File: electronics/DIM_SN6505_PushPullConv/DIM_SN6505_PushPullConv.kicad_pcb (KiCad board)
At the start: 2 copper layers, 31.3 x 13.4 mm, 18 parts, among them J1 Conn_01x04, J2 Conn_01x04, J3 Conn_01x04, J4 Conn_01x04, T1 STR7040, U1 SN6506A

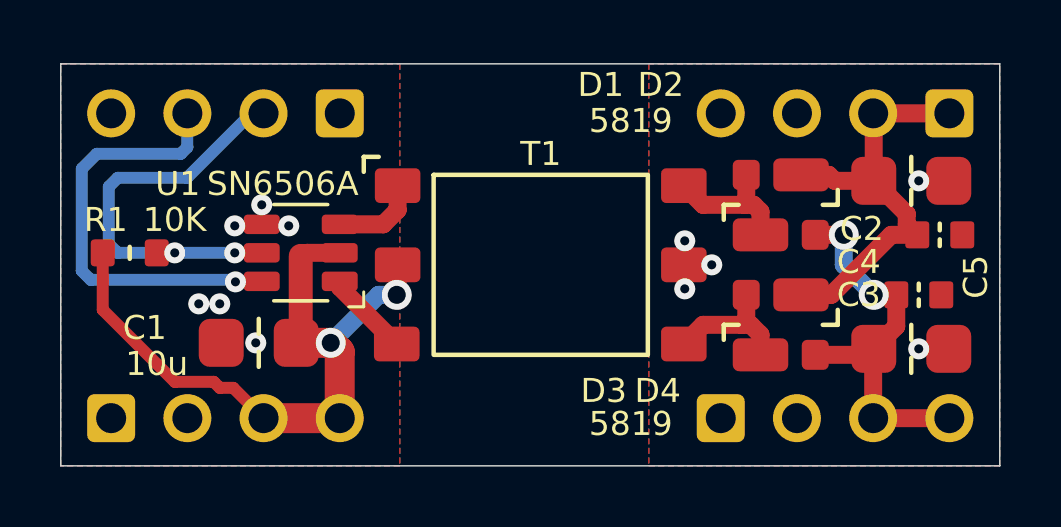
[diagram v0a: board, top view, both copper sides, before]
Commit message: renamed and cleaned up SN6505 breakout
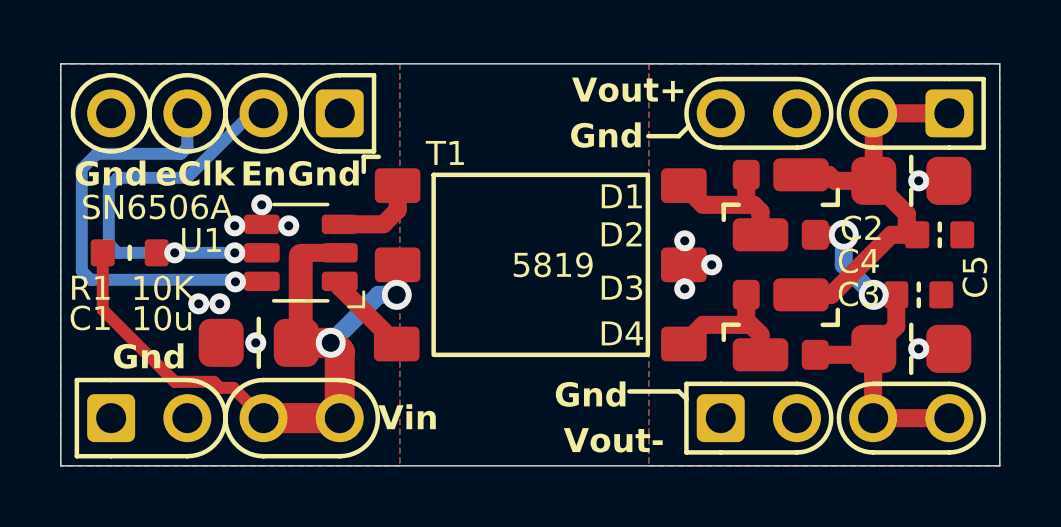
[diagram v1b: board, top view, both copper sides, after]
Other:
- board text added: "En"
- board text added: "Gnd"
- board text added: "Vin"
- board text added: "Vout+"
- board text added: "Vout-"
- board text added: "eClk"

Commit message: Updated VPS8701 DIM, fixed ERC/DRC
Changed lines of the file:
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@@
+	)
+	(gr_line
+		(start 138.43 81.28)
+		(end 138.43 83.82)
+		(stroke
+			(width 0.15)
+			(type default)
+		)
+		(layer "F.SilkS")
 	)
 	(gr_line
@@
 	)
 	(gr_line
-		(start 139.7 81.28)
+		(start 138.43 81.28)
 		(end 140.843 81.28)
 		(stroke
@@
 		(layer "F.SilkS")
 	)
-	(gr_arc
-		(start 139.7 83.82)
-		(mid 138.43 82.55)
-		(end 139.7 81.28)
-		(stroke
-			(width 0.15)
-			(type default)
-		)
-		(layer "F.SilkS")
-	)
 	(gr_line
 		(start 157.48 93.853)
@@
 	(gr_line
 		(start 140.843 83.82)
-		(end 139.7 83.82)
+		(end 138.43 83.82)
 		(stroke
 			(width 0.15)

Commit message: preparation for production V20260118
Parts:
- N1: value 20251002 -> 20260118
- moved C1 126.1 mm to (26.6, 29.3)
- moved C3 126.1 mm to (48.4, 29.5)
- moved N2 126.1 mm to (25.5, 26.0)
- moved U1 126.1 mm to (28.0, 26.3)
- moved C2 126.1 mm to (48.4, 23.9)
- moved C4 126.1 mm to (48.6, 27.7)
- moved D1 126.1 mm to (44.0, 23.7)
- moved D2 126.1 mm to (44.0, 25.7)
- moved D3 126.1 mm to (44.0, 27.7)
- moved D4 126.1 mm to (44.0, 29.7)
- moved J2 126.1 mm to (25.5, 21.6)
- moved J3 126.1 mm to (45.8, 31.8)
- moved J4 126.1 mm to (45.8, 21.6)
- moved N1 126.1 mm to (25.5, 29.7)
- moved R1 126.1 mm to (22.3, 26.3)
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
